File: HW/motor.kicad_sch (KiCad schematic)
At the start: 0 parts

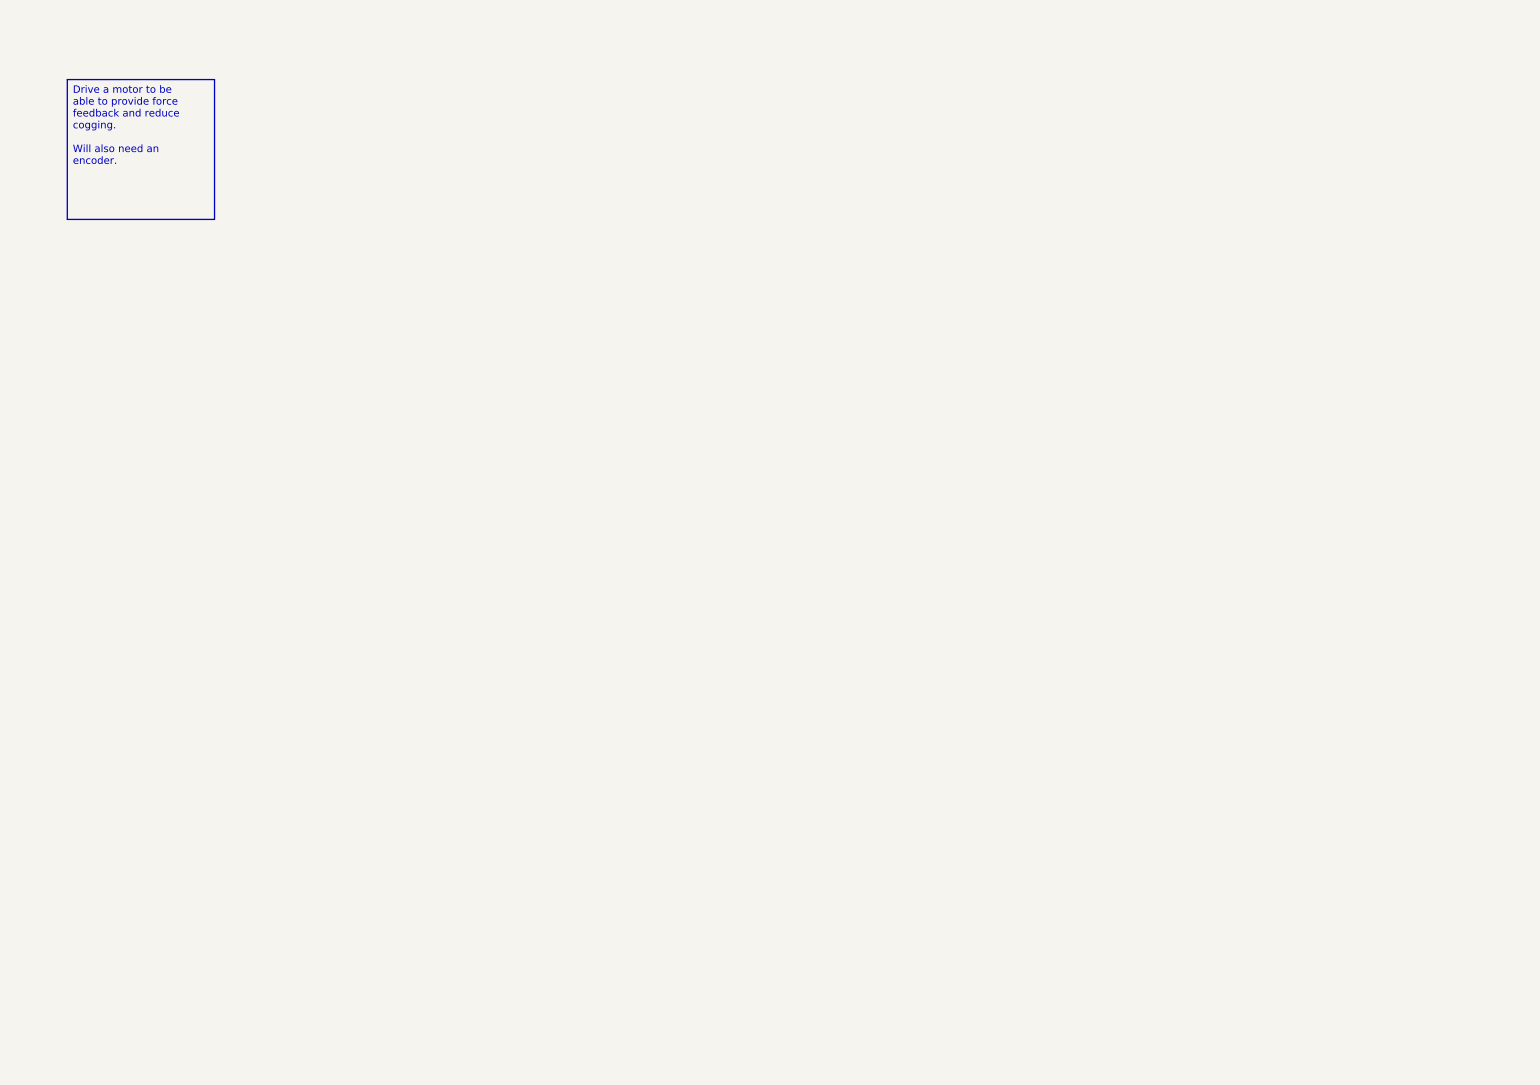
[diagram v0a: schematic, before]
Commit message: Almost first schematic draft (missing resistor values for STDRIVE current sensing and leds)
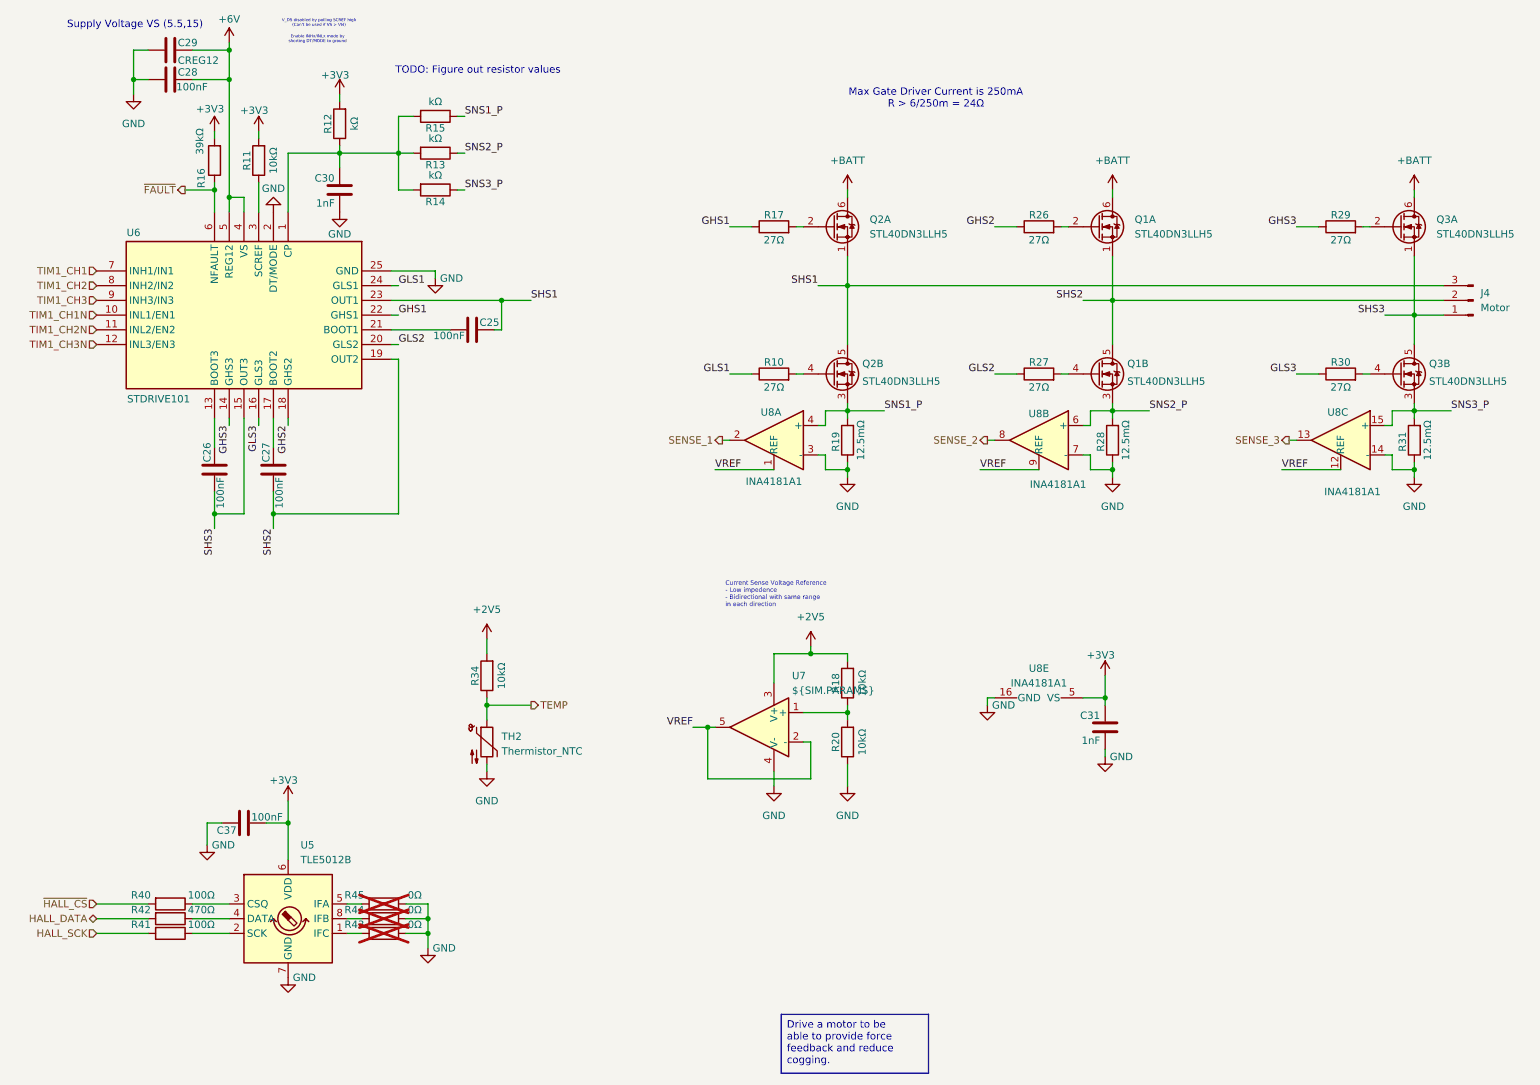
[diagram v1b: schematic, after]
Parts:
- added C25, C26, C27, C28, C37: 100nF, Capacitor_SMD:C_0402_1005Metric, symbol Device:C
- added C29: CREG12, Capacitor_SMD:C_0402_1005Metric, symbol Device:C
- added C30, C31: 1nF, Capacitor_SMD:C_0402_1005Metric, symbol Device:C
- added J4: Motor, symbol Connector:Conn_01x03_Pin
- added Q1, Q2, Q3: STL40DN3LLH5, lib:STL40DN3LLH5, symbol STL40DN3LLH5:STL40DN3LLH5
- added R10, R17, R26, R27, R29, R30: 27Ω, Resistor_SMD:R_0402_1005Metric, symbol Device:R
- added R11, R18, R20, R34: 10kΩ, Resistor_SMD:R_0402_1005Metric, symbol Device:R
- added R12, R13, R14, R15: kΩ, Resistor_SMD:R_0402_1005Metric, symbol Device:R
- added R16: 39kΩ, Resistor_SMD:R_0402_1005Metric, symbol Device:R
- added R19, R28, R31: 12.5mΩ, Resistor_SMD:R_0402_1005Metric, symbol Device:R
- added R40, R41: 100Ω, Resistor_SMD:R_0402_1005Metric, symbol Device:R
- added R42: 470Ω, Resistor_SMD:R_0402_1005Metric, symbol Device:R
- added R43, R44, R45: 0Ω, Resistor_SMD:R_0402_1005Metric, symbol Device:R
- added TH2: Thermistor_NTC, symbol Device:Thermistor_NTC
- added U5: TLE5012B, Package_SO:SOIC-8_3.9x4.9mm_P1.27mm, symbol Sensor_Magnetic:TLE5012B
- added U6: STDRIVE101, Package_DFN_QFN:QFN-24-1EP_4x4mm_P0.5mm_EP2.8x2.8mm_ThermalVias, symbol STDRIVE101:STDRIVE101
- added U7: ${SIM.PARAMS}, symbol Simulation_SPICE:OPAMP
- added U8: INA4181A1, Package_SO:TSSOP-20_4.4x6.5mm_P0.65mm, symbol lib:INA4181A1
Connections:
- new net: Q3.4 (G), R30.2
- new net: Q2.2 (G), R17.2
- new net: C30.1, R12.1, R13.2, R14.2, R15.2, U6.1 (CP)
- new net: R43.2, U5.1 (IFC)
- new net: Q1.2 (G), R26.2
- new net: C26.1, U6.13 (BOOT3)
- new net: C27.1, U6.17 (BOOT2)
- new net: C25.2, U6.21 (BOOT1)
- new net: R11.1, U6.3 (SCREF)
- new net: Q1.4 (G), R27.2
- new net: R40.1, U5.3 (CSQ)
- new net: R18.1, R20.2, U7.1 (+)
- new net: Q2.4 (G), R10.2
- new net: R44.2, U5.8 (IFB)
- new net: R45.2, U5.5 (IFA)
- new net: R42.1, U5.4 (DATA)
- new net: R41.1, U5.2 (SCK)
- new net: Q3.2 (G), R29.2
- new net +2V5: R18.2, R34.2, U7.3 (V+)
- new net +3V3: C31.1, C37.2, R11.2, R12.2, R16.2, U5.6 (VDD), U8.5 (VS)
- new net +6V: C28.1, C29.1, U6.4 (VS), U6.5 (REG12)
- new net +BATT: Q1.6 (D), Q2.6 (D), Q3.6 (D)
- new net GHS1: R17.1, U6.22 (GHS1)
- new net GHS2: R26.1, U6.18 (GHS2)
- new net GHS3: R29.1, U6.14 (GHS3)
- new net GLS1: R10.1, U6.24 (GLS1)
- new net GLS2: R27.1, U6.20 (GLS2)
- new net GLS3: R30.1, U6.16 (GLS3)
- new net GND: C28.2, C29.2, C30.2, C31.2, C37.1, R19.1, R20.1, R28.1, R31.1, R43.1, R44.1, R45.1, TH2.2, U5.7 (GND), U6.2 (DT/MODE), U6.25 (GND), U7.4 (V-), U8.14 (-), U8.16 (GND), U8.3 (-), U8.7 (-)
- new net HALL_DATA: R42.2
- new net HALL_SCK: R41.2
- new net SENSE_1: U8.2
- new net SENSE_2: U8.8
- new net SENSE_3: U8.13
- new net SHS1: C25.1, J4.3 (Pin_3), Q2.1 (S), Q2.5 (D), U6.23 (OUT1)
- new net SHS2: C27.2, J4.2 (Pin_2), Q1.1 (S), Q1.5 (D), U6.19 (OUT2)
- new net SHS3: C26.2, J4.1 (Pin_1), Q3.1 (S), Q3.5 (D), U6.15 (OUT3)
- new net SNS1_P: Q2.3 (S), R15.1, R19.2, U8.4 (+)
- new net SNS2_P: Q1.3 (S), R13.1, R28.2, U8.6 (+)
- new net SNS3_P: Q3.3 (S), R14.1, R31.2, U8.15 (+)
- new net TEMP: R34.1, TH2.1
- new net TIM1_CH1: U6.7 (INH1/IN1)
- new net TIM1_CH1N: U6.10 (INL1/EN1)
- new net TIM1_CH2: U6.8 (INH2/IN2)
- new net TIM1_CH2N: U6.11 (INL2/EN2)
- new net TIM1_CH3: U6.9 (INH3/IN3)
- new net TIM1_CH3N: U6.12 (INL3/EN3)
- new net VREF: U7.2 (-), U7.5, U8.1 (REF), U8.12 (REF), U8.9 (REF)
- new net ~{FAULT}: R16.1, U6.6 (NFAULT)
- new net ~{HALL_CS}: R40.2
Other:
- note added: "Current Sense Voltage Reference - Low impedence - Bidirectional with same range in each direction"
- note added: "Enable INHx/INLx mode by shorting DT/MODE to ground"
- note added: "Max Gate Driver Current is 250mA R > 6/250m = 24Ω"
- note added: "Supply Voltage VS (5.5,15)"
- note added: "TODO: Figure out resistor values"
- note added: "V_DS disabled by pulling SCREF high (Can't be used if VS > VM)"

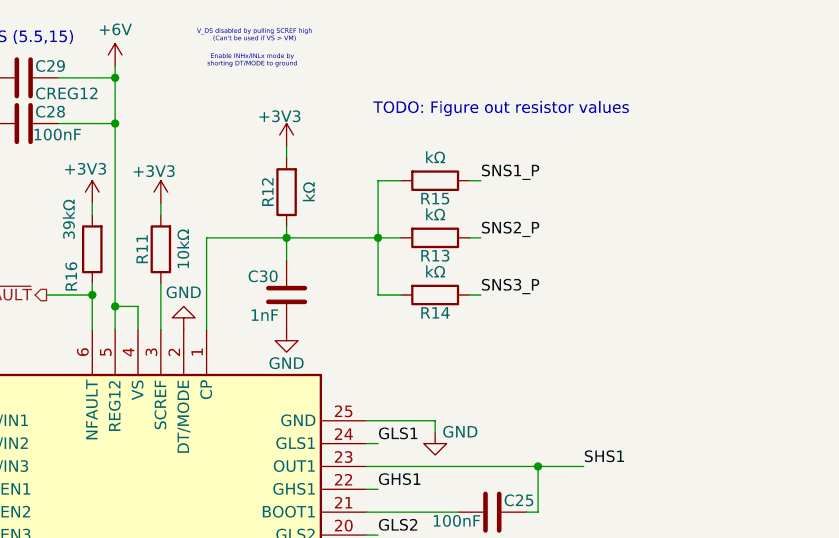
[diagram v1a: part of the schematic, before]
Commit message: Added resistor values for LED and removed STDRIVE current sensing
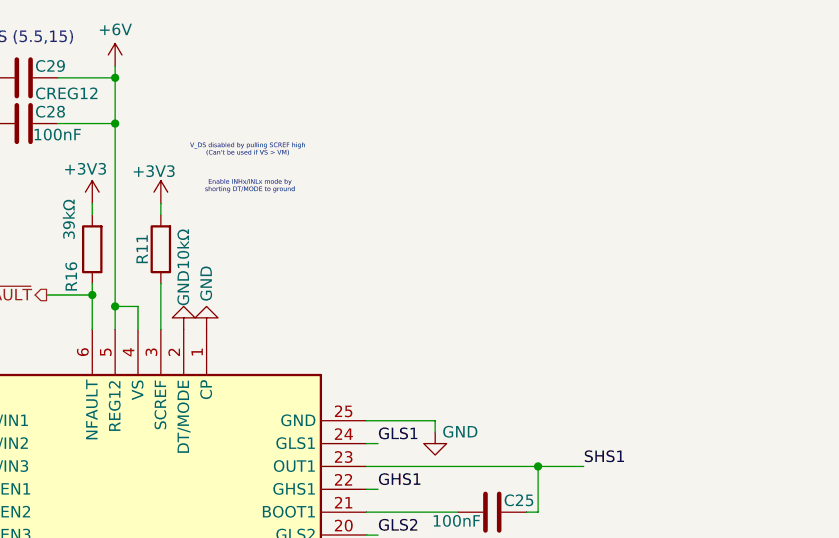
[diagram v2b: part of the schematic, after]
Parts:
- removed C30: 1nF, Capacitor_SMD:C_0402_1005Metric, symbol Device:C
- removed R12, R13, R14, R15: kΩ, Resistor_SMD:R_0402_1005Metric, symbol Device:R
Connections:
- net GND: now also U6.1 (CP)
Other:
- note removed: "TODO: Figure out resistor values"

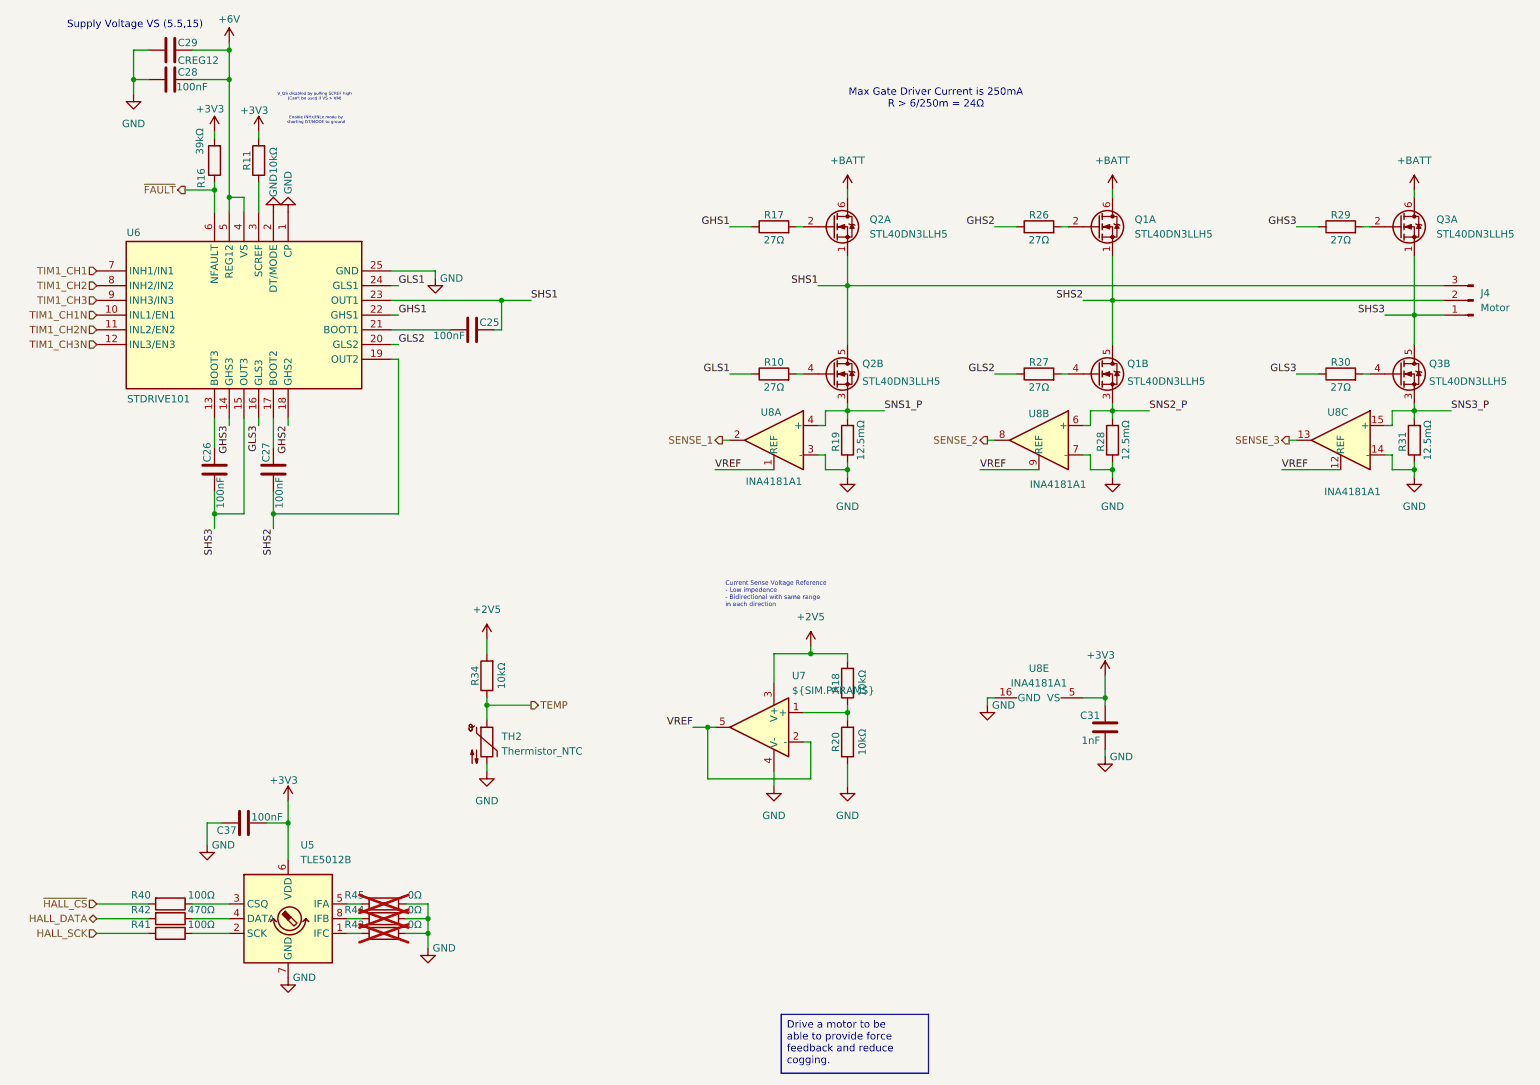
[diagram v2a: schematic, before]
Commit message: Cleaned up and implemented some of Laimonas' feedback
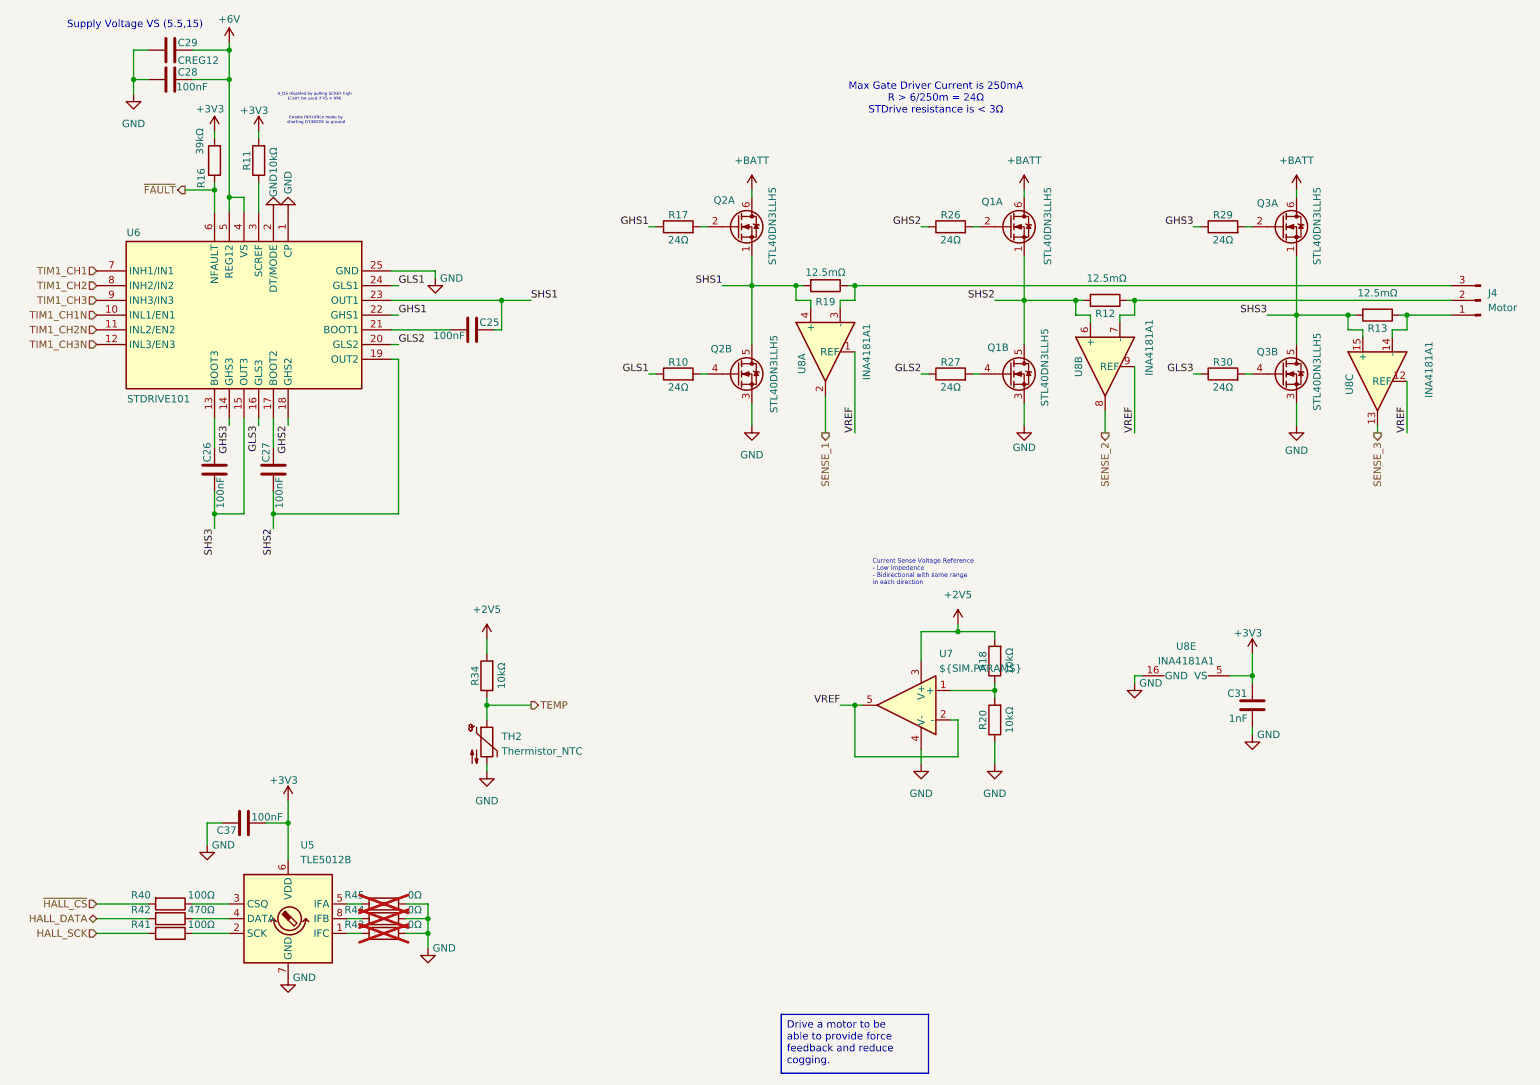
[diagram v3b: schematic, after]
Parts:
- removed R28, R31: 12.5mΩ, Resistor_SMD:R_0402_1005Metric, symbol Device:R
- added R12, R13: 12.5mΩ, Resistor_SMD:R_0402_1005Metric, symbol Device:R
- R10, R17, R26, R27, R29, R30: value 27Ω -> 24Ω
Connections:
- net GND: now also Q1.3 (S), Q2.3 (S), Q3.3 (S); no longer R19.1, U8.14 (-), U8.3 (-), U8.7 (-)
- net SHS1: now also R19.2, U8.4 (+); no longer J4.3 (Pin_3)
- net SHS2: now also U8.6 (+), R12.2; no longer J4.2 (Pin_2)
- net SHS3: now also U8.15 (+), R13.2; no longer J4.1 (Pin_1)
- removed net SNS1_P: Q2.3 (S), R19.2, U8.4 (+)
- removed net SNS2_P: Q1.3 (S), U8.6 (+)
- removed net SNS3_P: Q3.3 (S), U8.15 (+)
- new net: J4.2 (Pin_2), R12.1, U8.7 (-)
- new net: J4.1 (Pin_1), R13.1, U8.14 (-)
- new net: J4.3 (Pin_3), R19.1, U8.3 (-)
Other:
- note added: "Max Gate Driver Current is 250mA R > 6/250m = 24Ω STDrive resistance is < 3Ω"
- note removed: "Max Gate Driver Current is 250mA R > 6/250m = 24Ω"
- company: (none) -> Roberto Holmes
- title: (none) -> Capstan
- moved on the sheet: C31, J4, Q1A, Q1B, Q2A, Q2B, Q3A, Q3B, R10, R17, R18, R19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
